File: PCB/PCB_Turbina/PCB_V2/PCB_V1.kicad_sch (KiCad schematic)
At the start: 13 parts, among them J1 BATT_11.1V, J2 Conn_01x07, J3 ENODER_LEFT, J4 ENODER_RIGH, J5 BATT_7.4V, J6 JST-7.7V, J7 TURBINE_POWER, J8 TURBINE_PWM, SW1 Switch, U1 WeMos_S2_mini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

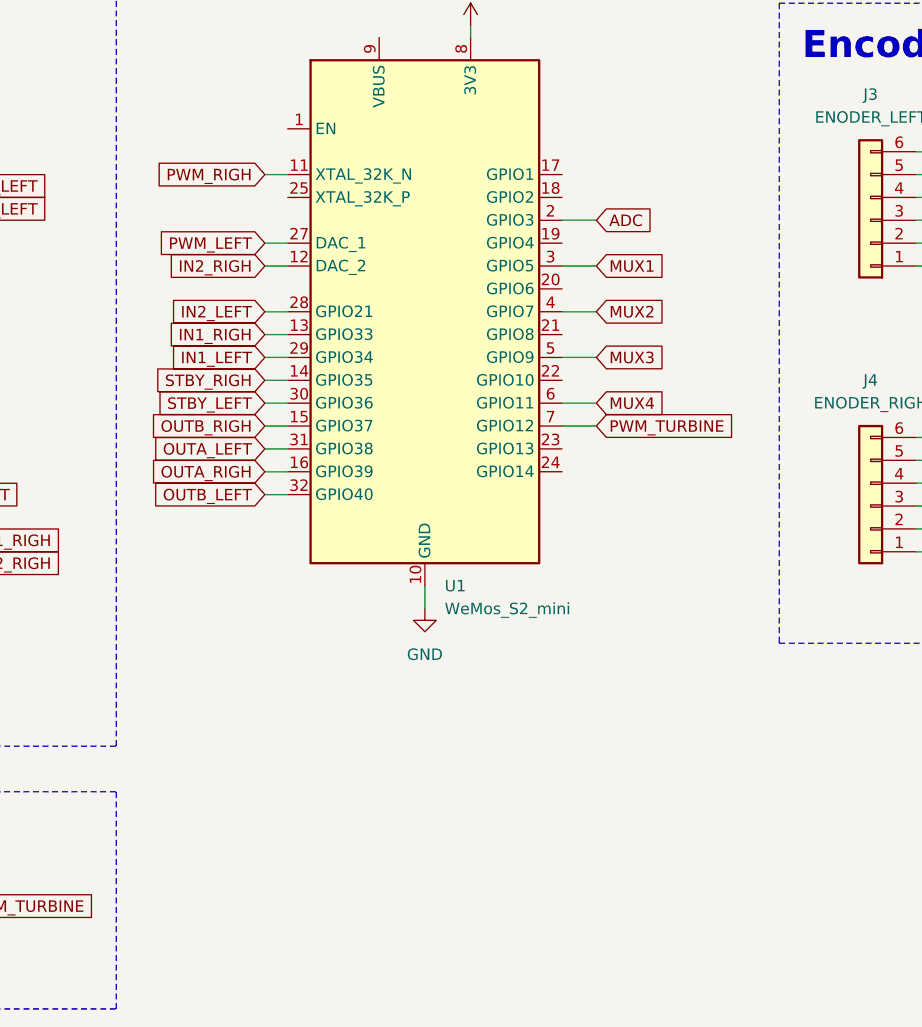
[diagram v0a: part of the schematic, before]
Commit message: Correccion modulo arranque PCB
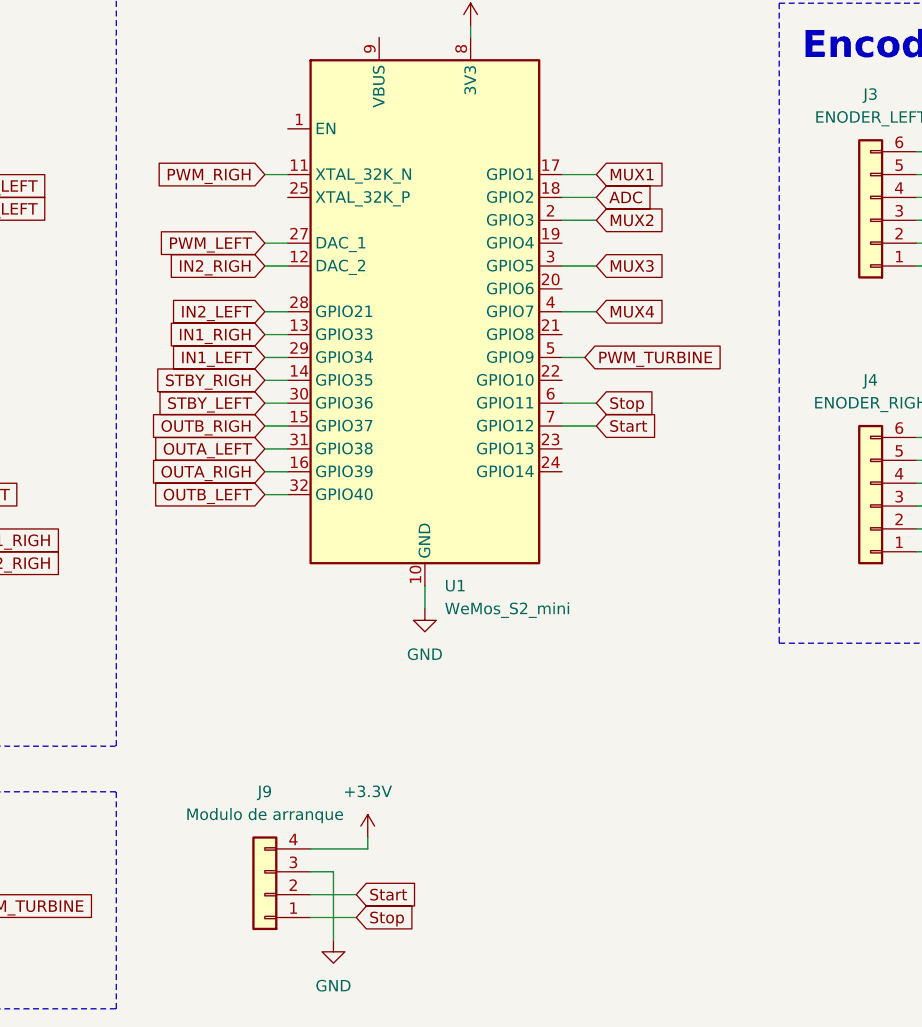
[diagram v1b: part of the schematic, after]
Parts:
- added J9: Modulo de arranque, Connector_PinHeader_2.54mm:PinHeader_1x04_P2.54mm_Vertical, symbol Connector_Generic:Conn_01x04
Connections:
- net +3.3V: now also J9.4 (Pin_4)
- net ADC: now also U1.18 (GPIO2); no longer U1.2 (GPIO3)
- net GND: now also J9.3 (Pin_3)
- net MUX1: now also U1.17 (GPIO1); no longer U1.3 (GPIO5)
- net MUX2: now also U1.2 (GPIO3); no longer U1.4 (GPIO7)
- net MUX3: now also U1.3 (GPIO5); no longer U1.5 (GPIO9)
- net MUX4: now also U1.4 (GPIO7); no longer U1.6 (GPIO11)
- net PWM_TURBINE: now also U1.5 (GPIO9); no longer U1.7 (GPIO12)
- new net Start: J9.2 (Pin_2), U1.7 (GPIO12)
- new net Stop: J9.1 (Pin_1), U1.6 (GPIO11)

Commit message: PCB_V3
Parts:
- removed J9: Modulo de arranque, Connector_PinHeader_2.54mm:PinHeader_1x04_P2.54mm_Vertical, symbol Connector_Generic:Conn_01x04
- removed U4: LM1117T-3.3, Package_TO_SOT_THT:TO-220-3_Horizontal_TabDown, symbol Regulator_Linear:LM1117T-3.3
- added J10: Conn_01x04, Connector_PinHeader_2.54mm:PinHeader_1x04_P2.54mm_Vertical, symbol Connector_Generic:Conn_01x04
- added J9: Conn_01x03, Connector_PinHeader_2.54mm:PinHeader_1x03_P2.54mm_Vertical, symbol Connector_Generic:Conn_01x03
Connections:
- net Start is gone; now on net MUX4: U1.7 (GPIO12)
- net Stop is gone; now on net MUX3: U1.6 (GPIO11)
- net +3.3V: now also J3.1 (Pin_1), J10.1 (Pin_1), J9.2 (Pin_2); no longer J3.2 (Pin_2)
- net 7.4V: now also J6.3 (Pin_3); no longer J6.4 (Pin_4)
- net ADC: now also U1.3 (GPIO5); no longer U1.18 (GPIO2)
- net BATT: now also J9.3 (Pin_3)
- net GND: now also J3.2 (Pin_2), J4.6 (Pin_6), J6.1 (Pin_1), J10.2 (Pin_2), J9.1 (Pin_1); no longer J3.1 (Pin_1), J4.4 (Pin_4), J6.2 (Pin_2)
- net IN1_LEFT: now also U1.15 (GPIO37); no longer U1.29 (GPIO34)
- net IN1_RIGH: now also U1.29 (GPIO34); no longer U1.13 (GPIO33)
- net IN2_LEFT: now also U1.14 (GPIO35); no longer U1.28 (GPIO21)
- net IN2_RIGH: now also U1.28 (GPIO21); no longer U1.12 (DAC_2)
- net M2_RIGH: now also J4.4 (Pin_4); no longer J4.6 (Pin_6)
- net MUX1: now also U1.4 (GPIO7); no longer U1.17 (GPIO1)
- net MUX2: now also U1.5 (GPIO9); no longer U1.2 (GPIO3)
- net MUX3: no longer U1.3 (GPIO5)
- net MUX4: no longer U1.4 (GPIO7)
- net OUTA_LEFT: now also U1.12 (DAC_2); no longer U1.31 (GPIO38)
- net OUTA_RIGH: now also J4.1 (Pin_1), U1.32 (GPIO40); no longer J4.2 (Pin_2), U1.16 (GPIO39)
- net OUTB_LEFT: now also U1.11 (XTAL_32K_N); no longer U1.32 (GPIO40)
- net OUTB_RIGH: now also J4.2 (Pin_2), U1.31 (GPIO38); no longer J4.1 (Pin_1), U1.15 (GPIO37)
- net PWM_LEFT: now also U1.13 (GPIO33); no longer U1.27 (DAC_1)
- net PWM_RIGH: now also U1.27 (DAC_1); no longer U1.11 (XTAL_32K_N)
- net PWM_TURBINE: now also U1.25 (XTAL_32K_P); no longer U1.5 (GPIO9)
- net STBY_LEFT: now also U1.16 (GPIO39); no longer U1.30 (GPIO36)
- net STBY_RIGH: now also U1.30 (GPIO36); no longer U1.14 (GPIO35)
- net START: now reaches U1.23 (GPIO13)
- net START: now also J10.3 (Pin_3)
- net STOP: now reaches U1.24 (GPIO14)
- net STOP: now also J10.4 (Pin_4)
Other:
- moved on the sheet: J6
